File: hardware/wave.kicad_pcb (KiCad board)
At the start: 4 copper layers, 60 x 60 mm, 123 parts, among them J101 CORTEX-DEBUG, J102 WAGO-2065, J103 WAGO-2065, J104 WAGO-2065, J105 WAGO-2065, J106 WAGO-2065, J107 WAGO-2065, J301 2x05_Horizontal, J401 2x05_Horizontal, J501 WAGO-2065, J502 WAGO-2065, Q201 IRF9358, SW101 SW_Push, SW102 SW_Push, U101 TPS78433QWDRBRQ1, U102 ATSAMD51J, U201 MA12070P, U301 THVD24x2, U401 THVD24x2, U501 74AHC1G125, Y101 32k768

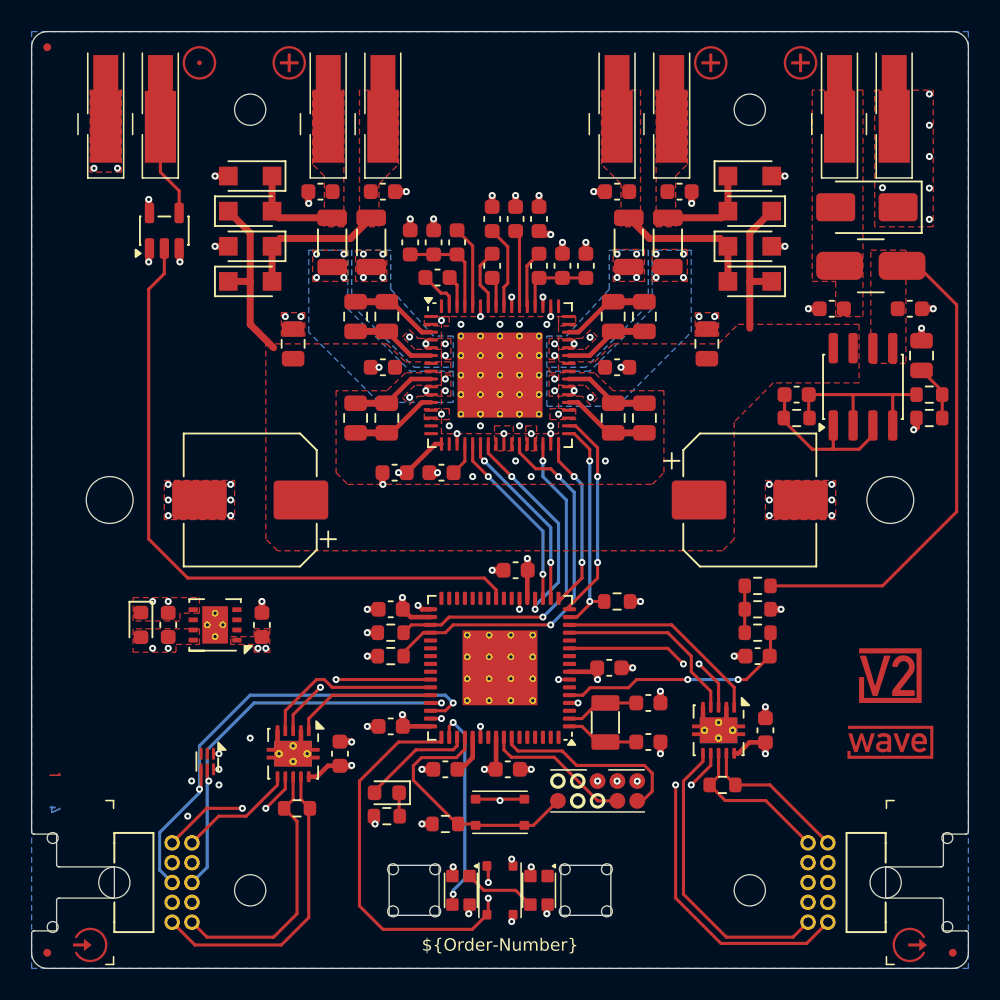
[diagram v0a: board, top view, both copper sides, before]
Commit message: Replace Order_Number
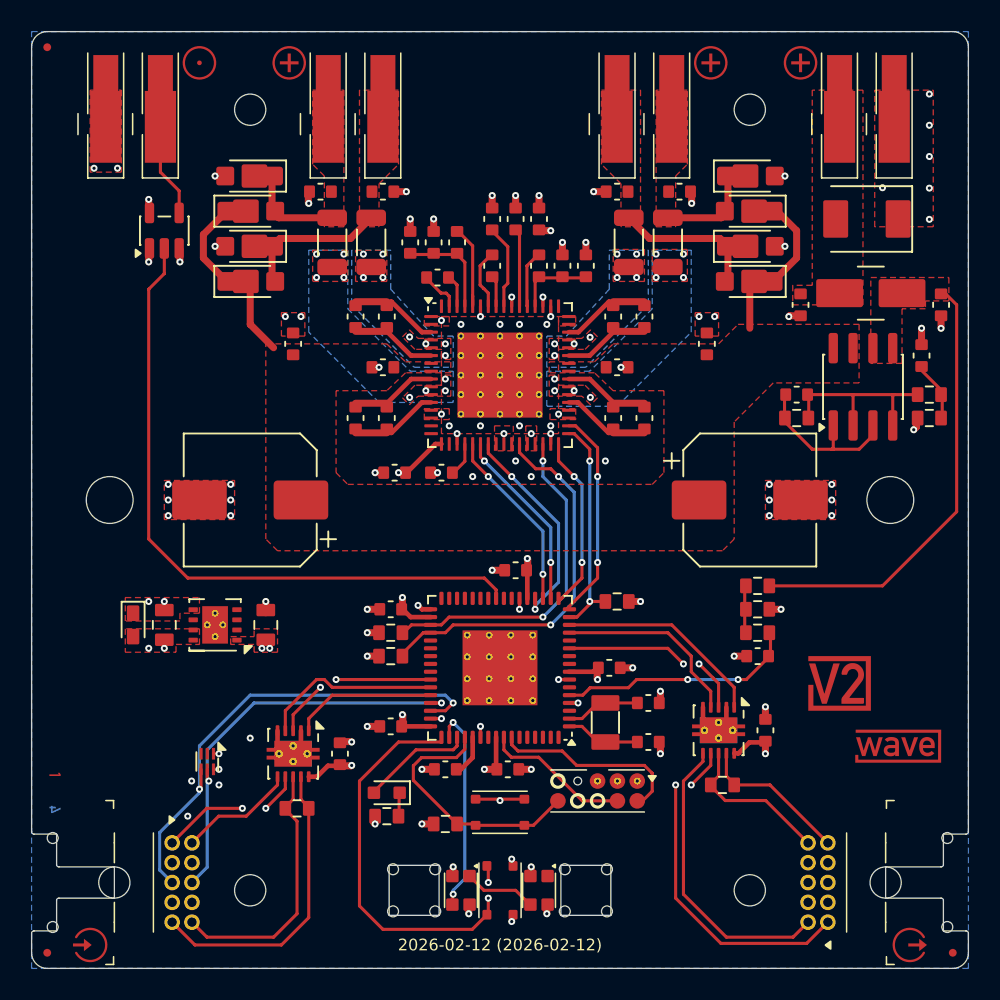
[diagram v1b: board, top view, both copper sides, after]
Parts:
- C101: renamed from C109; footprint Capacitor_SMD:C_0603_1608Metric -> V2_Capacitor_SMD:C_0603
- C102: renamed from C110; footprint Capacitor_SMD:C_0603_1608Metric -> V2_Capacitor_SMD:C_0603
- C103: renamed from C113; footprint Capacitor_SMD:C_0603_1608Metric -> V2_Capacitor_SMD:C_0603
- C104: renamed from C101; footprint Capacitor_SMD:C_0603_1608Metric -> V2_Capacitor_SMD:C_0603
- C105: renamed from C111; footprint Capacitor_SMD:C_0603_1608Metric -> V2_Capacitor_SMD:C_0603
- C106: renamed from C112; footprint Capacitor_SMD:C_0603_1608Metric -> V2_Capacitor_SMD:C_0603
- C107: renamed from C102; footprint Capacitor_SMD:C_0603_1608Metric -> V2_Capacitor_SMD:C_0603
- C108: renamed from C103; footprint Capacitor_SMD:C_0603_1608Metric -> V2_Capacitor_SMD:C_0603
- C109: renamed from C104; footprint Capacitor_SMD:C_0603_1608Metric -> V2_Capacitor_SMD:C_0603
- C110: renamed from C105; footprint Capacitor_SMD:C_0603_1608Metric -> V2_Capacitor_SMD:C_0603
- C111: renamed from C106; footprint Capacitor_SMD:C_0603_1608Metric -> V2_Capacitor_SMD:C_0603
- C112: renamed from C107; footprint Capacitor_SMD:C_0603_1608Metric -> V2_Capacitor_SMD:C_0805
- C113: renamed from C108; footprint Capacitor_SMD:C_0603_1608Metric -> V2_Capacitor_SMD:C_0805
- C201: renamed from C207; footprint Capacitor_SMD:C_0603_1608Metric -> V2_Capacitor_SMD:C_0603
- C202: renamed from C210; footprint Capacitor_SMD:C_0805_2012Metric -> V2_Capacitor_SMD:C_0603
- C203: renamed from C228; footprint Capacitor_SMD:C_0603_1608Metric -> V2_Capacitor_SMD:C_0603
- C204: renamed from C232; footprint Capacitor_SMD:C_0603_1608Metric -> V2_Capacitor_SMD:C_0603
- C205: renamed from C208; footprint Capacitor_SMD:C_0603_1608Metric -> V2_Capacitor_SMD:C_0603
- C206: renamed from C233; footprint Capacitor_SMD:C_0603_1608Metric -> V2_Capacitor_SMD:C_0603
- C207: renamed from C209; footprint Capacitor_SMD:C_0603_1608Metric -> V2_Capacitor_SMD:C_0603
- C208: renamed from C201; footprint Capacitor_SMD:C_0603_1608Metric -> V2_Capacitor_SMD:C_0603
- C209: renamed from C202; footprint Capacitor_SMD:C_0805_2012Metric -> V2_Capacitor_SMD:C_0603
- C210: renamed from C211; footprint Capacitor_SMD:C_0805_2012Metric -> V2_Capacitor_SMD:C_0603
- C211: renamed from C214; footprint Capacitor_SMD:C_0805_2012Metric -> V2_Capacitor_SMD:C_0603
- C212: renamed from C217; footprint Capacitor_SMD:C_0805_2012Metric -> V2_Capacitor_SMD:C_0603
- C213: renamed from C220; footprint Capacitor_SMD:C_0805_2012Metric -> V2_Capacitor_SMD:C_0603
- C214: renamed from C223; footprint Capacitor_SMD:C_0603_1608Metric -> V2_Capacitor_SMD:C_0603
- C215: renamed from C226; footprint Capacitor_SMD:C_0603_1608Metric -> V2_Capacitor_SMD:C_0603
- C216: renamed from C227; footprint Capacitor_SMD:C_0603_1608Metric -> V2_Capacitor_SMD:C_0603
- C217: renamed from C231; footprint Capacitor_SMD:C_0603_1608Metric -> V2_Capacitor_SMD:C_0603
- C218: renamed from C203; footprint Capacitor_SMD:CP_Elec_8x10 -> V2_Capacitor_SMD:CP_Elec_8x10
- C219: renamed from C212; footprint Capacitor_SMD:C_0805_2012Metric -> V2_Capacitor_SMD:C_0603
- C220: renamed from C215; footprint Capacitor_SMD:C_0805_2012Metric -> V2_Capacitor_SMD:C_0603
- C221: renamed from C218; footprint Capacitor_SMD:C_0805_2012Metric -> V2_Capacitor_SMD:C_0603
- C222: renamed from C221; footprint Capacitor_SMD:C_0805_2012Metric -> V2_Capacitor_SMD:C_0603
- C223: renamed from C224; footprint Capacitor_SMD:C_0603_1608Metric -> V2_Capacitor_SMD:C_0603
- C224: renamed from C229; footprint Capacitor_SMD:C_0603_1608Metric -> V2_Capacitor_SMD:C_0603
- C225: renamed from C204; footprint Capacitor_SMD:C_0603_1608Metric -> V2_Capacitor_SMD:C_0603
- C226: renamed from C225; footprint Capacitor_SMD:C_0603_1608Metric -> V2_Capacitor_SMD:C_0603
- C227: renamed from C230; footprint Capacitor_SMD:C_0603_1608Metric -> V2_Capacitor_SMD:C_0603
- C228: renamed from C205; footprint Capacitor_SMD:C_0805_2012Metric -> V2_Capacitor_SMD:C_0603
- C229: renamed from C213; footprint Capacitor_SMD:C_0603_1608Metric -> V2_Capacitor_SMD:C_0603
- C230: renamed from C216; footprint Capacitor_SMD:C_0603_1608Metric -> V2_Capacitor_SMD:C_0603
- C231: renamed from C219; footprint Capacitor_SMD:C_0603_1608Metric -> V2_Capacitor_SMD:C_0603
- C232: renamed from C222; footprint Capacitor_SMD:C_0603_1608Metric -> V2_Capacitor_SMD:C_0603
- C233: renamed from C206; footprint Capacitor_SMD:CP_Elec_8x10 -> V2_Capacitor_SMD:CP_Elec_8x10
- C301, C401: footprint Capacitor_SMD:C_0603_1608Metric -> V2_Capacitor_SMD:C_0603
- D101: footprint LED_SMD:LED_0603_1608Metric -> V2_LED:LED_0603
- D201, D208: value PMEG3010ER -> PMEG6030AEXEX; footprint Diode_SMD:Nexperia_CFP3_SOD-123W -> V2_Diode_SMD:D_SOD-123HP
- D202: renamed from D203; value PMEG3010ER -> PMEG6030AEXEX; footprint Diode_SMD:Nexperia_CFP3_SOD-123W -> V2_Diode_SMD:D_SOD-123HP
- D203: renamed from D205; value PMEG3010ER -> PMEG6030AEXEX; footprint Diode_SMD:Nexperia_CFP3_SOD-123W -> V2_Diode_SMD:D_SOD-123HP
- D204: renamed from D207; value PMEG3010ER -> PMEG6030AEXEX; footprint Diode_SMD:Nexperia_CFP3_SOD-123W -> V2_Diode_SMD:D_SOD-123HP
- D205: renamed from D202; value PMEG3010ER -> PMEG6030AEXEX; footprint Diode_SMD:Nexperia_CFP3_SOD-123W -> V2_Diode_SMD:D_SOD-123HP
- D206: renamed from D204; value PMEG3010ER -> PMEG6030AEXEX; footprint Diode_SMD:Nexperia_CFP3_SOD-123W -> V2_Diode_SMD:D_SOD-123HP
- D207: renamed from D206; value PMEG3010ER -> PMEG6030AEXEX; footprint Diode_SMD:Nexperia_CFP3_SOD-123W -> V2_Diode_SMD:D_SOD-123HP
- FB101: value 47R -> 47 Ohm
- FB201, FB202, FB203, FB204: value 50R -> 50 Ohm; footprint Inductor_SMD:L_1206_3216Metric -> V2_Inductor_SMD:L_1206
- FID101, FID102, FID103: value Fiducial -> Fiducial_Paste
- H101: value MountingHole_2mm -> 2mm
- H102: renamed from H103; value MountingHole_2mm -> 2mm
- H103: renamed from H105; value MountingHole_2mm -> 2mm
- H104: renamed from H106; value MountingHole_2mm -> 2mm
- H105: renamed from H102; value MountingHole_3mm -> 3mm
- H106: renamed from H104; value MountingHole_3mm -> 3mm
- INFO101: renamed from INFO102; value ORDER-NUMBER -> ~; footprint V2_Production:Order_Number -> V2_Production:Revision
- J101: renamed from J102; value WAGO-2065 -> WAGO 2065-100
- J102: renamed from J105; value WAGO-2065 -> WAGO 2065-100
- J103: renamed from J101; value CORTEX-DEBUG -> Cortex; footprint V2_Cortex_Debug:Cortex_Debug_Pad -> V2_Connector_Debug:Cortex
- J104: renamed from J103; value WAGO-2065 -> WAGO 2065-100
- J105: renamed from J104; value WAGO-2065 -> WAGO 2065-100
- J106, J107, J501, J502: value WAGO-2065 -> WAGO 2065-100
- Q201: footprint Package_SO:SOIC-8_3.9x4.9mm_P1.27mm -> V2_Package_SO:SOIC-8_3.9x4.9mm_P1.27mm
- R101: renamed from R105; footprint Resistor_SMD:R_0603_1608Metric -> V2_Resistor_SMD:R_0603
- R102: renamed from R108; footprint Resistor_SMD:R_0603_1608Metric -> V2_Resistor_SMD:R_0603
- R103: renamed from R106; footprint Resistor_SMD:R_0603_1608Metric -> V2_Resistor_SMD:R_0603
- R104: renamed from R102; footprint Resistor_SMD:R_0603_1608Metric -> V2_Resistor_SMD:R_0603
- R105: renamed from R103; footprint Resistor_SMD:R_0603_1608Metric -> V2_Resistor_SMD:R_0603
- R106: renamed from R104; footprint Resistor_SMD:R_0603_1608Metric -> V2_Resistor_SMD:R_0603
- R107, R201, R202, R203, R301, R401: footprint Resistor_SMD:R_0603_1608Metric -> V2_Resistor_SMD:R_0603
- R108: renamed from R101; footprint Resistor_SMD:R_0603_1608Metric -> V2_Resistor_SMD:R_0603
- SW101: renamed from SW102; value SW_Push -> SKSG
- SW102: renamed from SW101; value SW_Push -> SKSG
- TVS101: renamed from TVS102; value SMAJ24CA -> SMBJ24CA; footprint Diode_SMD:D_SMA -> V2_Diode_SMD:D_SMB
- TVS102: renamed from TVS101; footprint Diode_SMD:D_0603_1608Metric -> V2_Diode_SMD:D_0603
- U301, U401: value THVD24x2 -> THVD2442
- U501: footprint Package_TO_SOT_SMD:SOT-23-5 -> V2_Package_TO_SOT_SMD:SOT-23-5
- moved ICON102 3.29 mm to (118.8, 96.8)
- moved C105 2.02 mm to (116.2, 72.5), turned to -90 degrees
- moved C106 2.02 mm to (125.2, 72.5), turned to -90 degrees
- moved FB101 1.75 mm to (120.8, 71.8)
- moved TVS101 0.75 mm to (120.5, 67.0)
- moved ICON101 0.56 mm to (122.5, 100.8)
- moved TVS102 0.50 mm to (73.5, 93.0)
- moved C112 0.25 mm to (75.5, 93.0)
- moved C113 0.25 mm to (82.0, 93.0)
- renumbered ICON108 to ICON101, ICON107 to ICON102, ICON101 to ICON103, ICON102 to ICON105, ICON105 to ICON106, ICON103 to ICON107, ICON106 to ICON108, INFO101 to INFO102, U102 to U101, U101 to U102
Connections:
- net /Supply +24V renamed /+24V-Supply
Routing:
- net /Power: track 31.7 -> 28.4 mm
- net /Amplifier Audio/PVDD: track 20.8 -> 23.5 mm
- net GND: track 46.2 -> 46.0 mm, vias 102 -> 100
- net +3V3: vias 15 -> 14

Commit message: Update Library
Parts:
- FB101: value 47 Ohm -> ~
- FB201, FB202, FB203, FB204: value 50 Ohm -> ~
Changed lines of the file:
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@@
 			)
 		)
-		(property "Value" "50 Ohm"
+		(property "Value" "~"
 			(at 0 1.9 90)
 			(layer "F.Fab")
@@
 			)
 		)
-		(property "Value" "47 Ohm"
+		(property "Value" "~"
 			(at 0 2.9 0)
 			(layer "F.Fab")
@@
 			)
 		)
-		(property "Value" "50 Ohm"
+		(property "Value" "~"
 			(at 0 1.9 90)
 			(layer "F.Fab")
@@
 			)
 		)
-		(property "Value" "50 Ohm"
+		(property "Value" "~"
 			(at 0 1.9 90)
 			(layer "F.Fab")
@@
 		)
 		(group ""
-			(members "4532dc4e-f69d-412b-bc19-695d90100dcb" "8f0d22e3-918a-451d-a4a3-d23b9b599883"
-				"ae9bfc19-817d-4f4b-b84f-b22dd92c01e5" "bdaa4d0f-ab94-4c16-8f20-3c5ec3e83d21"
-				"f26a1357-79ae-4b96-a7f4-25831135af06"
+			(members "817afe4d-3ef8-4f34-841e-a1e0d13acd88" "8d5b3521-d299-4149-812d-e93ed26aa732"
+				"add876ea-4949-4e26-8186-7559bdf5a9eb" "b58fdfc9-b605-4197-b451-9f65004c44a9"
+				"c6308024-9361-453b-adb7-b5cdd279d357"
 			)
 		)
 		(group ""
-			(members "17461222-e6b8-4a40-a234-68067f321262" "96fa0783-c83b-424a-9582-f57065f0b73f"
-				"9e55e1cf-c869-4549-9032-91aab361908b" "9ef00dd0-bc50-46b7-b0af-3ca977389725"
-				"dabd2c8a-06ea-4384-a9f6-28d395331438"
+			(members "3d585795-267e-4acf-9233-fa6d3d19a673" "a58be4f5-7508-488d-900a-1671a0babb7c"
+				"bce2bd36-7243-4190-8a23-6d6964d44d4c" "e52a77fc-53a3-4bee-8404-ef76a262d8b0"
+				"fb6306f7-0653-42ec-a4a8-a7408847cb8f"
 			)
 		)
@@
 			)
 		)
-		(property "Value" "50 Ohm"
+		(property "Value" "~"
 			(at 0 1.9 90)
 			(layer "F.Fab")

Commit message: Update
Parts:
- FB101: value ~ -> 47 Ω
- FB201, FB202, FB203, FB204: value ~ -> 50 Ω
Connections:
- net /Amplifier Audio/PVDD renamed /Amplifier Audio/+PVDD
- net Net-(Q201A-G1) renamed /Amplifier Audio/Gate
- net Net-(Q201A-S1) renamed /Amplifier Audio/Source
- C105 pad 1: /+24V-Supply -> /+24V
- C106 pad 1: /Power -> /+24V-Supply
- FB101 pad 1: /+24V-Supply -> /+24V
- FB101 pad 2: /Power -> /+24V-Supply
- J101 pad 1: /+24V-Supply -> /+24V
- Q201 pad 5: /Power -> /+24V-Supply
- Q201 pad 6: /Power -> /+24V-Supply
- R101 pad 1: /Power -> /+24V-Supply
- TVS101 pad 2: /+24V-Supply -> /+24V
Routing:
- net /Power: track 28.4 -> 0.00 mm
- net /+24V-Supply: track 0.00 -> 28.4 mm
- net /Amplifier Audio/Source: track 10.8 -> 12.4 mm
- added copper zone on F.Cu, net /+24V
- removed copper zone on F.Cu, net /Power
